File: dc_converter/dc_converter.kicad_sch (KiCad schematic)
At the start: 41 parts, among them IC1 A3946KLPTR-T, IC2 NCV20072DMR2G, J1 xt30Con, J2 xt30Con, J3 Conn_01x09_Pin, Q1 CSD18531Q5A, Q2 CSD18531Q5A, Q3 CSD18531Q5A, U1 LM74700, U3 INA280A2xDCK, U4 INA280A2xDCK

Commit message: Added 2 simulink concepts, with high and low sides mosfets
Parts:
- R1, R2: footprint Resistor_SMD:R_0402_1005Metric -> Resistor_SMD:R_1206_3216Metric_Pad1.30x1.75mm_HandSolder
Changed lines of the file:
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@@
 			)
 		)
-		(property "Footprint" "Resistor_SMD:R_0402_1005Metric"
+		(property "Footprint" "Resistor_SMD:R_1206_3216Metric_Pad1.30x1.75mm_HandSolder"
 			(at 127 74.168 90)
 			(hide yes)
@@
 			)
 		)
-		(property "Footprint" "Resistor_SMD:R_0402_1005Metric"
+		(property "Footprint" "Resistor_SMD:R_1206_3216Metric_Pad1.30x1.75mm_HandSolder"
 			(at 127 99.568 90)
 			(hide yes)

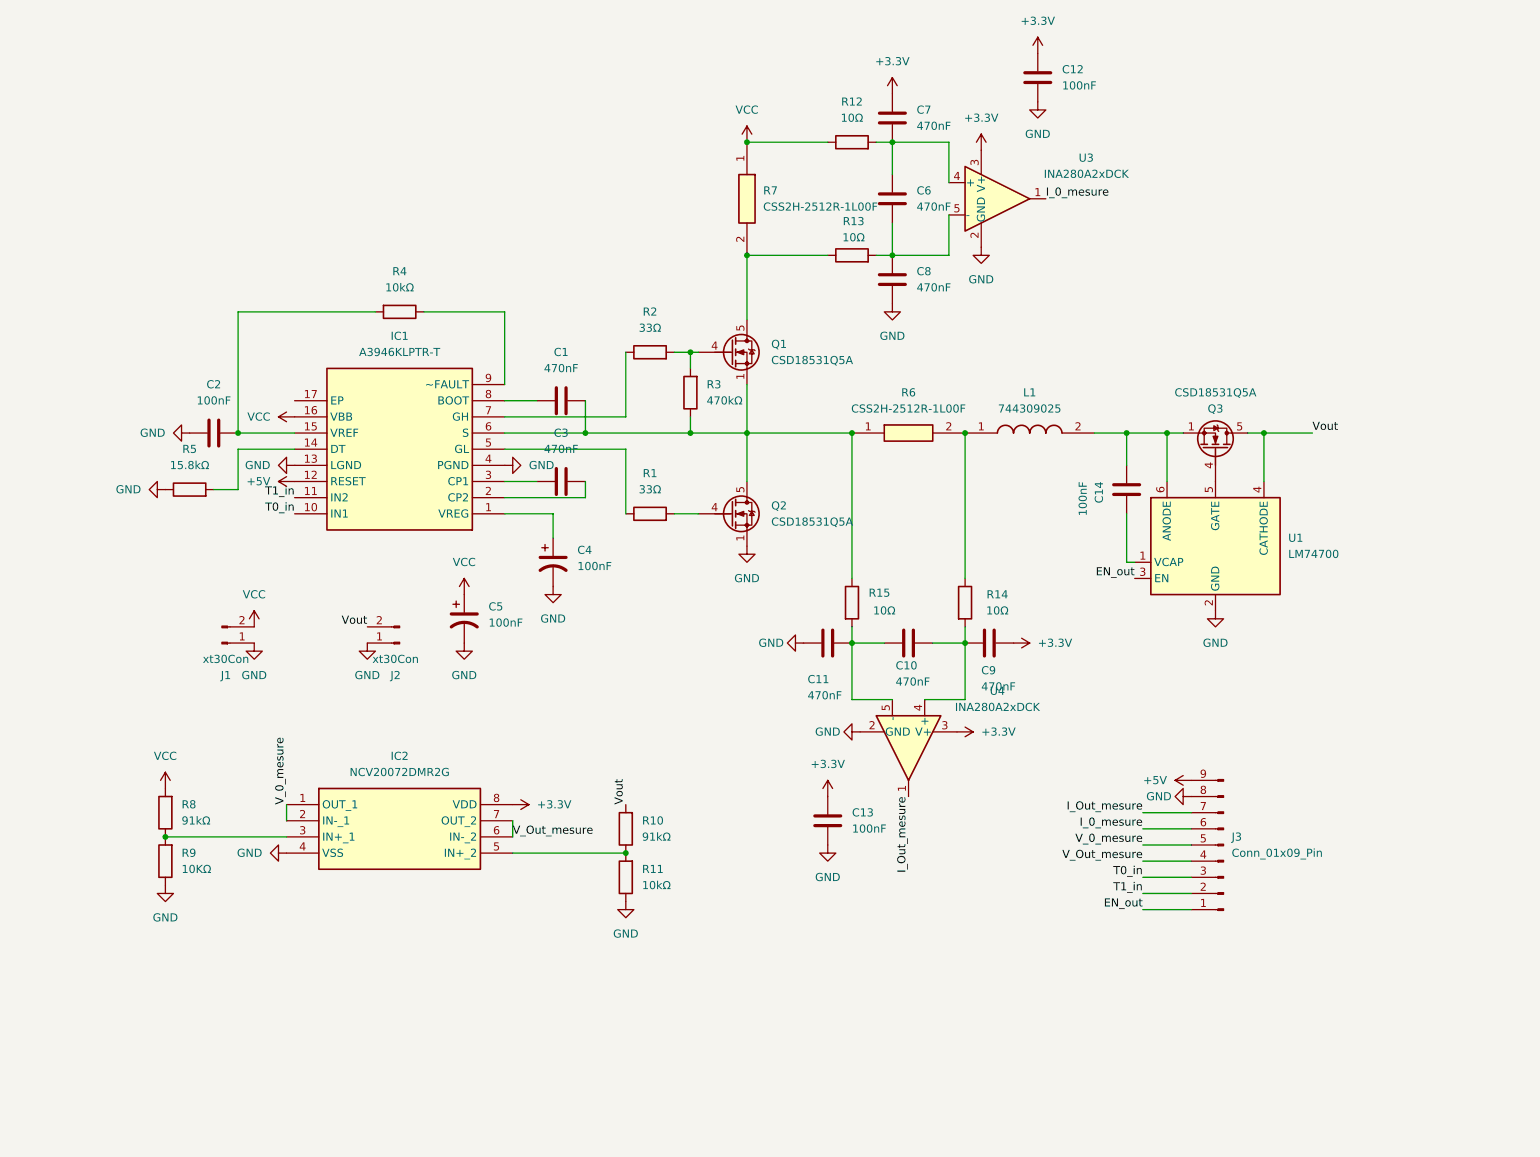
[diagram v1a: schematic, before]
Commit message: Full topology change to the circuit, diode for Q2, new L, new driver, topology changes in simulink
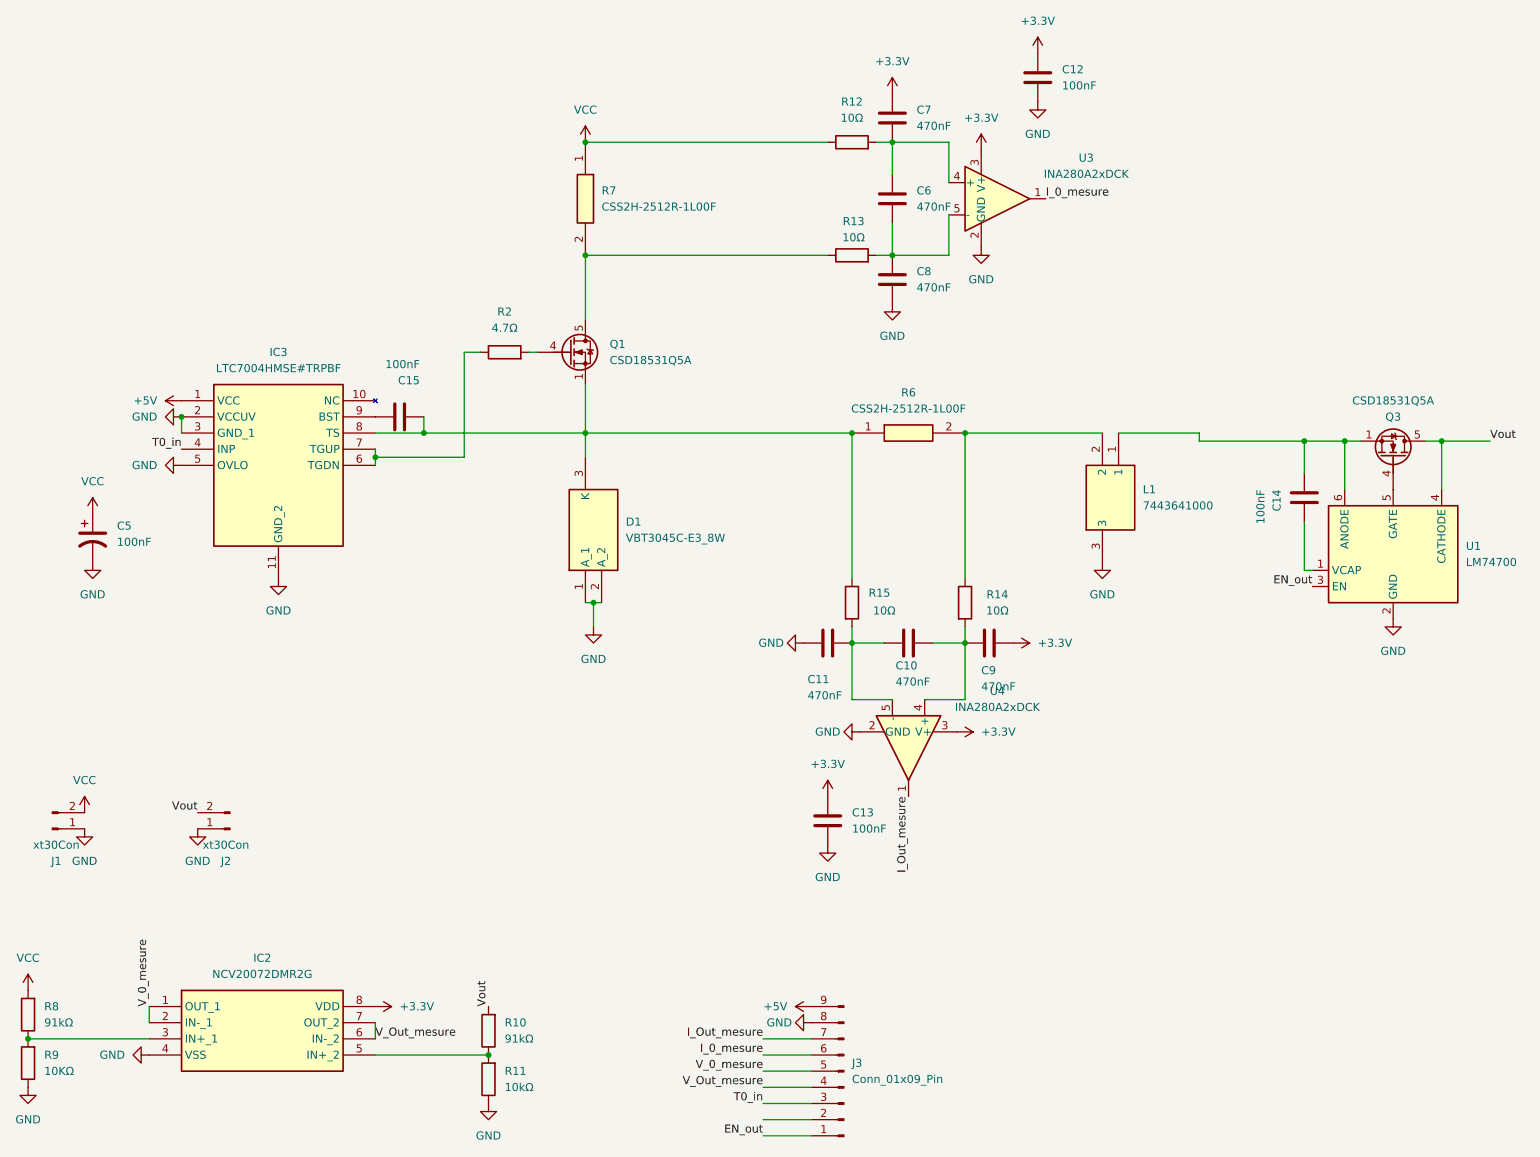
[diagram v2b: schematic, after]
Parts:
- removed C1, C3: 470nF, Capacitor_SMD:C_0402_1005Metric, symbol Device:C
- removed C2: 100nF, Capacitor_SMD:C_0402_1005Metric, symbol Device:C
- removed C4: 100nF, symbol Device:C_Polarized_US
- removed IC1: A3946KLPTR-T, A2550KLPTRT, symbol A3946KLPTR-T:A3946KLPTR-T
- removed L1: 744309025, INDPM140130X900N, symbol 744309025:744309025
- removed Q2: CSD18531Q5A, Package_TO_SOT_SMD:TDSON-8-1, symbol Transistor_FET:CSD18531Q5A
- removed R1: 33Ω, Resistor_SMD:R_1206_3216Metric_Pad1.30x1.75mm_HandSolder, symbol Device:R
- removed R3: 470kΩ, Resistor_SMD:R_0402_1005Metric, symbol Device:R
- removed R4: 10kΩ, Resistor_SMD:R_0402_1005Metric, symbol Device:R
- removed R5: 15.8kΩ, Resistor_SMD:R_0402_1005Metric, symbol Device:R
- added C15: 100nF, Capacitor_SMD:C_0402_1005Metric, symbol Device:C
- added D1: VBT3045C-E3_8W, TO-263AB_1, symbol VBT3045C-E3_8W:VBT3045C-E3_8W
- added IC3: LTC7004HMSE#TRPBF, SOP50P490X110-11N, symbol LTC7004HMSE#TRPBF:LTC7004HMSE#TRPBF
- added L1: 7443641000, WE-HCF_SMD_HIGH-CURRENT_INDUCTOR, symbol 7443641000:7443641000
- R2: value 33Ω -> 4.7Ω
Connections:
- net +5V: now also IC3.1 (VCC)
- net GND: now also D1.1 (A_1), D1.2 (A_2), IC3.11 (GND_2), IC3.2 (VCCUV), IC3.3 (GND_1), IC3.5 (OVLO), L1.3
- net T0_in: now also IC3.4 (INP)
- net at Q1.1 (S), Q1.2 (S), Q1.3 (S)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: now also C15.1, D1.3 (K), IC3.8 (TS)
- net at C14.1, Q3.1 (S), Q3.2 (S)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: now also L1.1
- net at R14.1, R6.2: now also L1.2
- net at R2.1: now also IC3.6 (TGDN), IC3.7 (TGUP)
- net T1_in: no longer names the net of J3.2 (Pin_2)
- new net: C15.2, IC3.9 (BST)
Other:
- moved on the sheet: C14, C5, IC2, J1, J2, J3, Q1, Q3, R10, R11, R2, R7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
